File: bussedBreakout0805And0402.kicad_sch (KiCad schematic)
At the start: 46 parts, among them J1 Conn_01x12_Pin, J10 Conn_01x06_Pin, J11 Conn_01x06_Pin, J12 Conn_01x06_Pin, J13 Conn_01x06_Pin, J14 Conn_01x06_Pin, J15 Conn_01x06_Pin, J16 Conn_01x06_Pin, J17 Conn_01x06_Pin, J18 Conn_01x06_Pin, J19 Conn_01x06_Pin, J2 Conn_01x01_Pin, J20 Conn_01x06_Pin, J21 Conn_01x06_Pin, J22 Conn_01x06_Pin, J23 Conn_01x06_Pin, J24 Conn_01x06_Pin, J25 Conn_01x06_Pin, J26 Conn_01x06_Pin, J27 Conn_01x06_Pin, J28 Conn_01x06_Pin, J29 Conn_01x06_Pin, J3 Conn_01x01_Pin, J30 Conn_01x06_Pin, J31 Conn_01x06_Pin, J32 Conn_01x06_Pin, J4 Conn_01x05_Pin, J5 Conn_01x05_Pin, J6 Conn_01x01_Pin, J7 Conn_01x01_Pin, J8 Conn_01x12_Pin, J9 Conn_01x06_Pin

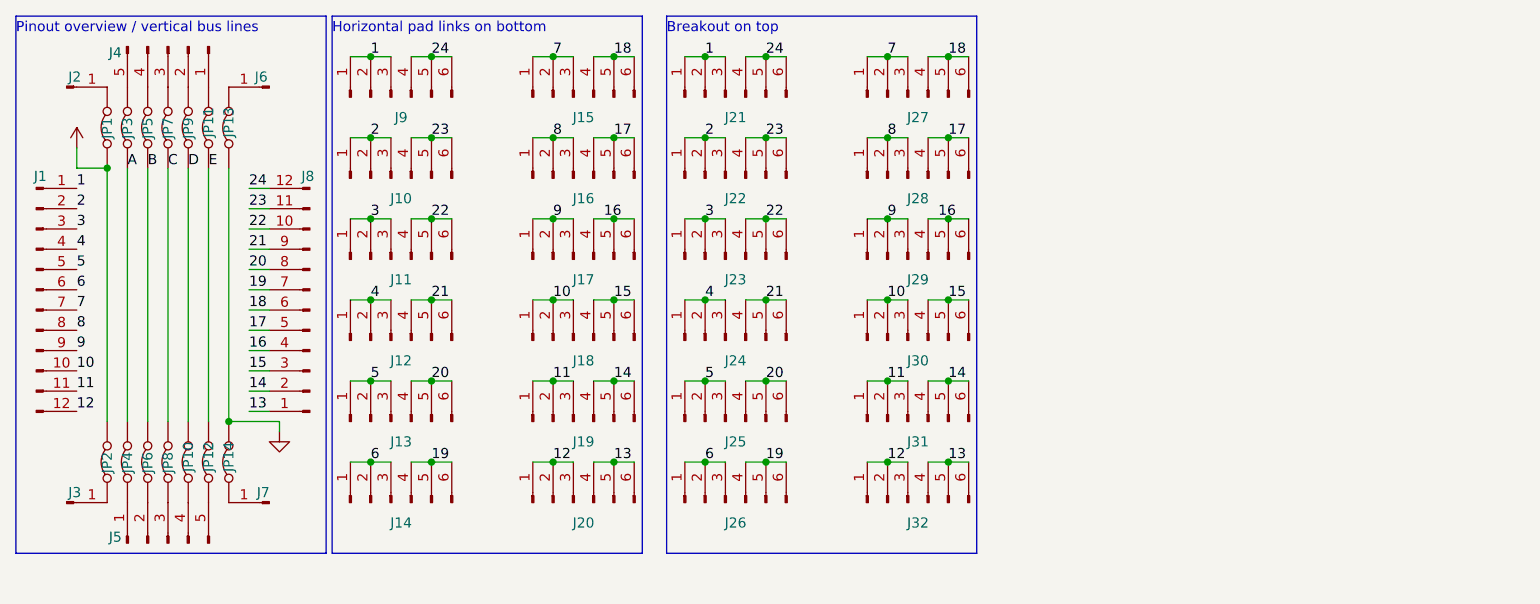
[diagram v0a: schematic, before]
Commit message: Replace 1/3 of top 0805 footprints with twice as many 0402 ones
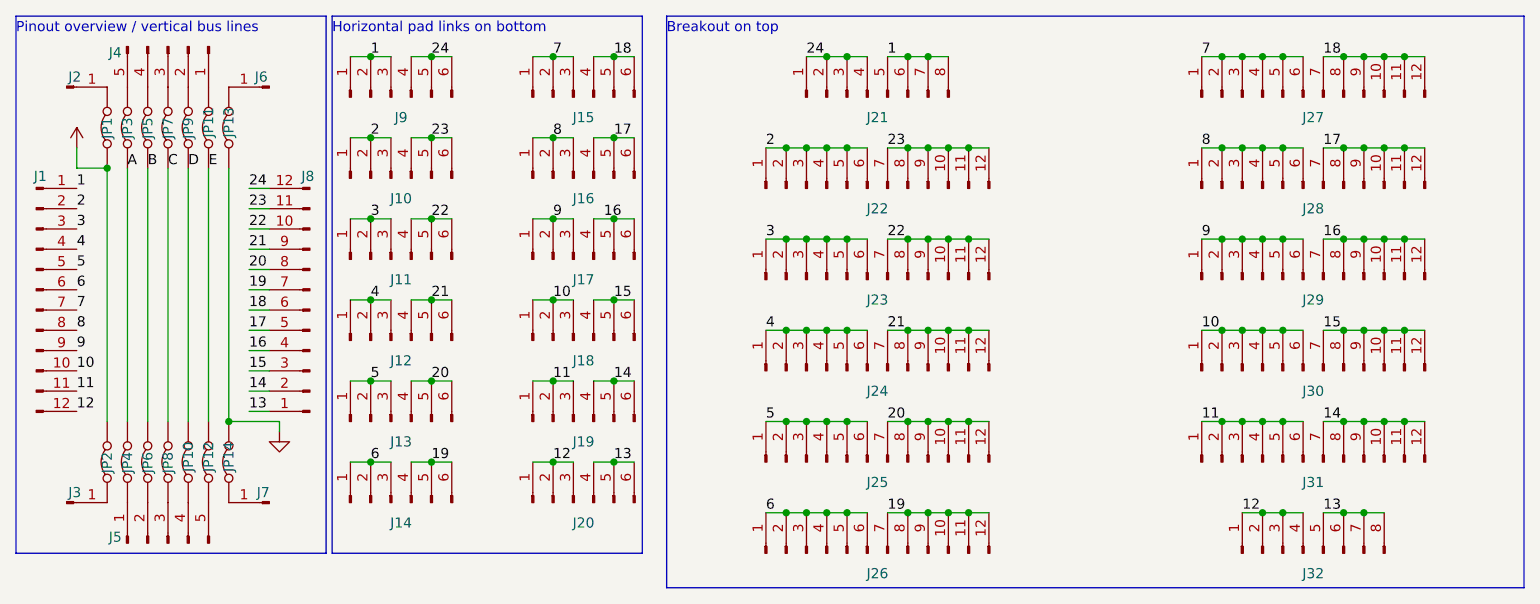
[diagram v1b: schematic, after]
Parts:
- removed J21, J22, J23, J24, J25, J26, J27, J28, J29, J30, J31, J32: Conn_01x06_Pin, SMD:SMD_0805_grid_1x6, symbol Connector:Conn_01x06_Pin
- added J21, J32: Conn_01x12_Pin, SMD:SMD_0805_grid_1x6_interleaved_0402_1x2, symbol Connector:Conn_01x08_Pin
- added J22, J23, J24, J25, J26, J27, J28, J29, J30, J31: Conn_01x20_Pin, SMD:SMD_0805_grid_1x6_interleaved_0402_2x2, symbol Connector:Conn_01x12_Pin
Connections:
- net 1: now also J21.5 (Pin_5), J21.6 (Pin_6), J21.7 (Pin_7), J21.8 (Pin_8)
- net 10: now also J30.1 (Pin_1), J30.2 (Pin_2), J30.3 (Pin_3), J30.4 (Pin_4), J30.5 (Pin_5), J30.6 (Pin_6)
- net 11: now also J31.1 (Pin_1), J31.2 (Pin_2), J31.3 (Pin_3), J31.4 (Pin_4), J31.5 (Pin_5), J31.6 (Pin_6)
- net 12: now also J32.1 (Pin_1), J32.2 (Pin_2), J32.3 (Pin_3), J32.4 (Pin_4)
- net 13: now also J32.5 (Pin_5), J32.6 (Pin_6), J32.7 (Pin_7), J32.8 (Pin_8)
- net 14: now also J31.10 (Pin_10), J31.11 (Pin_11), J31.12 (Pin_12), J31.7 (Pin_7), J31.8 (Pin_8), J31.9 (Pin_9)
- net 15: now also J30.10 (Pin_10), J30.11 (Pin_11), J30.12 (Pin_12), J30.7 (Pin_7), J30.8 (Pin_8), J30.9 (Pin_9)
- net 16: now also J29.10 (Pin_10), J29.11 (Pin_11), J29.12 (Pin_12), J29.7 (Pin_7), J29.8 (Pin_8), J29.9 (Pin_9)
- net 17: now also J28.10 (Pin_10), J28.11 (Pin_11), J28.12 (Pin_12), J28.7 (Pin_7), J28.8 (Pin_8), J28.9 (Pin_9)
- net 18: now also J27.10 (Pin_10), J27.11 (Pin_11), J27.12 (Pin_12), J27.7 (Pin_7), J27.8 (Pin_8), J27.9 (Pin_9)
- net 19: now also J26.10 (Pin_10), J26.11 (Pin_11), J26.12 (Pin_12), J26.7 (Pin_7), J26.8 (Pin_8), J26.9 (Pin_9)
- net 2: now also J22.1 (Pin_1), J22.2 (Pin_2), J22.3 (Pin_3), J22.4 (Pin_4), J22.5 (Pin_5), J22.6 (Pin_6)
- net 20: now also J25.10 (Pin_10), J25.11 (Pin_11), J25.12 (Pin_12), J25.7 (Pin_7), J25.8 (Pin_8), J25.9 (Pin_9)
- net 21: now also J24.10 (Pin_10), J24.11 (Pin_11), J24.12 (Pin_12), J24.7 (Pin_7), J24.8 (Pin_8), J24.9 (Pin_9)
- net 22: now also J23.10 (Pin_10), J23.11 (Pin_11), J23.12 (Pin_12), J23.7 (Pin_7), J23.8 (Pin_8), J23.9 (Pin_9)
- net 23: now also J22.10 (Pin_10), J22.11 (Pin_11), J22.12 (Pin_12), J22.7 (Pin_7), J22.8 (Pin_8), J22.9 (Pin_9)
- net 24: now also J21.1 (Pin_1), J21.2 (Pin_2), J21.3 (Pin_3), J21.4 (Pin_4)
- net 3: now also J23.1 (Pin_1), J23.2 (Pin_2), J23.3 (Pin_3), J23.4 (Pin_4), J23.5 (Pin_5), J23.6 (Pin_6)
- net 4: now also J24.1 (Pin_1), J24.2 (Pin_2), J24.3 (Pin_3), J24.4 (Pin_4), J24.5 (Pin_5), J24.6 (Pin_6)
- net 5: now also J25.1 (Pin_1), J25.2 (Pin_2), J25.3 (Pin_3), J25.4 (Pin_4), J25.5 (Pin_5), J25.6 (Pin_6)
- net 6: now also J26.1 (Pin_1), J26.2 (Pin_2), J26.3 (Pin_3), J26.4 (Pin_4), J26.5 (Pin_5), J26.6 (Pin_6)
- net 7: now also J27.1 (Pin_1), J27.2 (Pin_2), J27.3 (Pin_3), J27.4 (Pin_4), J27.5 (Pin_5), J27.6 (Pin_6)
- net 8: now also J28.1 (Pin_1), J28.2 (Pin_2), J28.3 (Pin_3), J28.4 (Pin_4), J28.5 (Pin_5), J28.6 (Pin_6)
- net 9: now also J29.1 (Pin_1), J29.2 (Pin_2), J29.3 (Pin_3), J29.4 (Pin_4), J29.5 (Pin_5), J29.6 (Pin_6)
